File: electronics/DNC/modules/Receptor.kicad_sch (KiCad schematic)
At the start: 19 parts

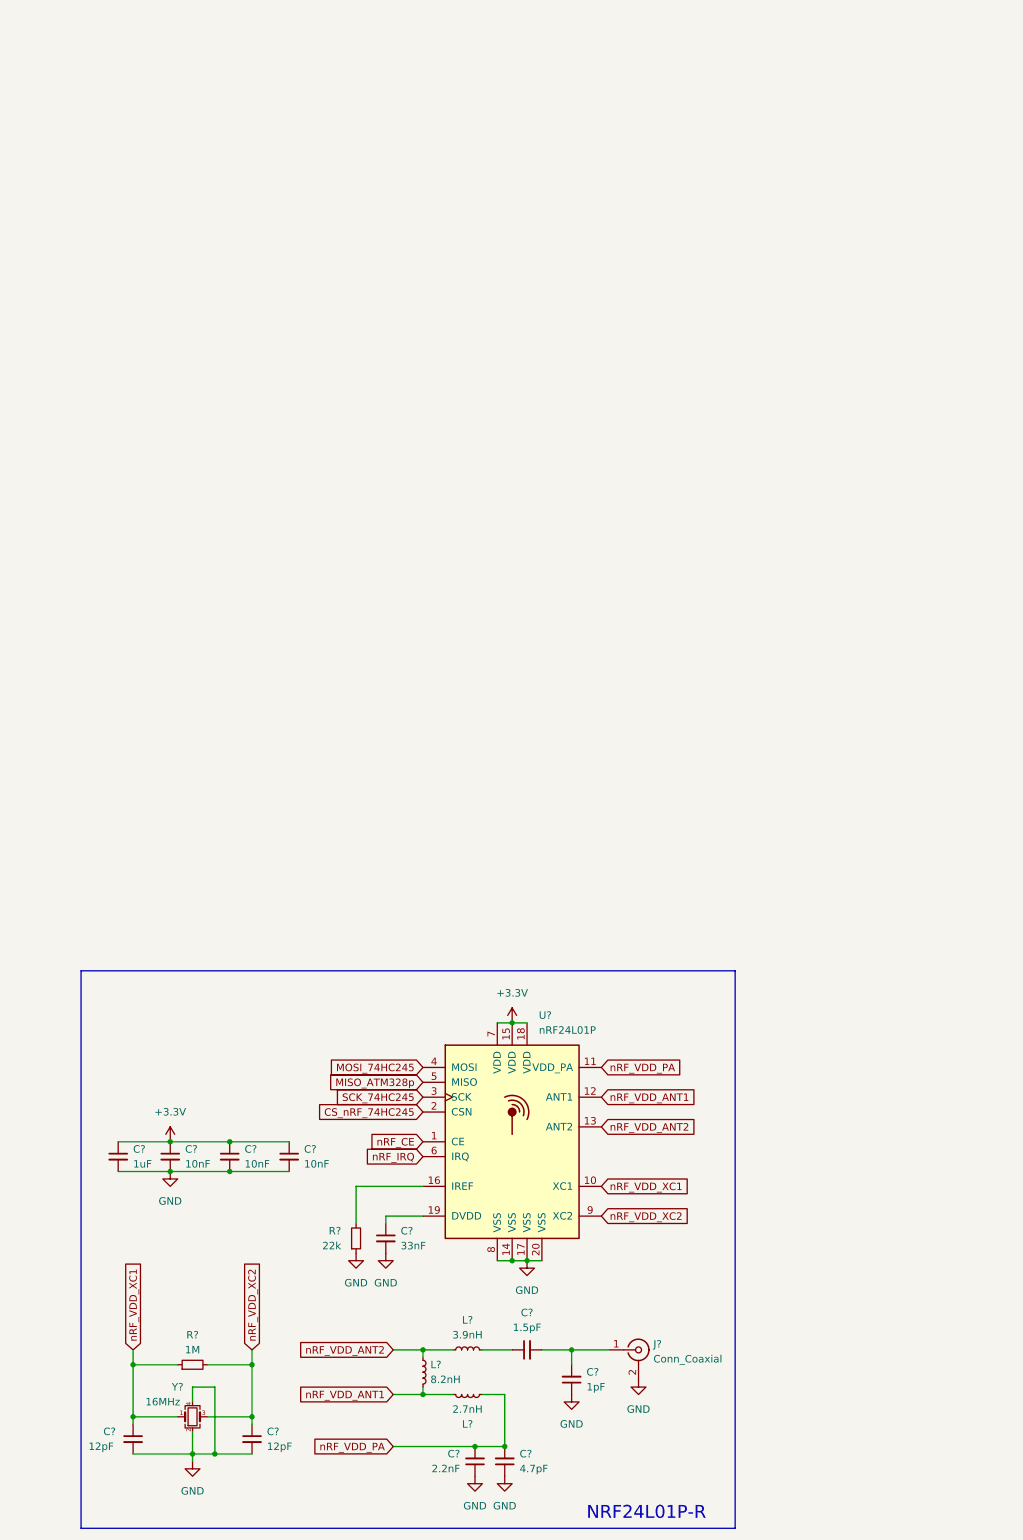
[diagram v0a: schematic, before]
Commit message: Se reemplazó la hoja del IMU por la de sensores y se agregó la hoja de indicadores
- Nueva hoja Sensores: IMU BMI270 (SPI1) y barómetro BMP581 (I2C1 propio, jumper BARO_ADDR).
- Nueva hoja Indicadores: buzzer piezo CPT-12123 con FDV303N y LEDs de estado en PB4/PB5.
- Se eliminó la hoja IMU.
- MicroSD por SDIO de 4 bits con filtro TPD6F002 y TVS ESD5Z3.3 en VDD.
- PMS: AP2112K en 3V3_SYS y LP5907 + ferrita en 3V3_SEN.
- Motores movidos a PA0-PA3 (TIM5) para liberar el SDIO.
- Arquitectura.drawio actualizado a la arquitectura v1 (ELRS por UART, sin OLED).
- Se agregó docs/RESUMEN_PROYECTO_DNC.md con decisiones y pendientes.

Co-Authored-By: Claude Opus 5.5 <noreply@anthropic.com>
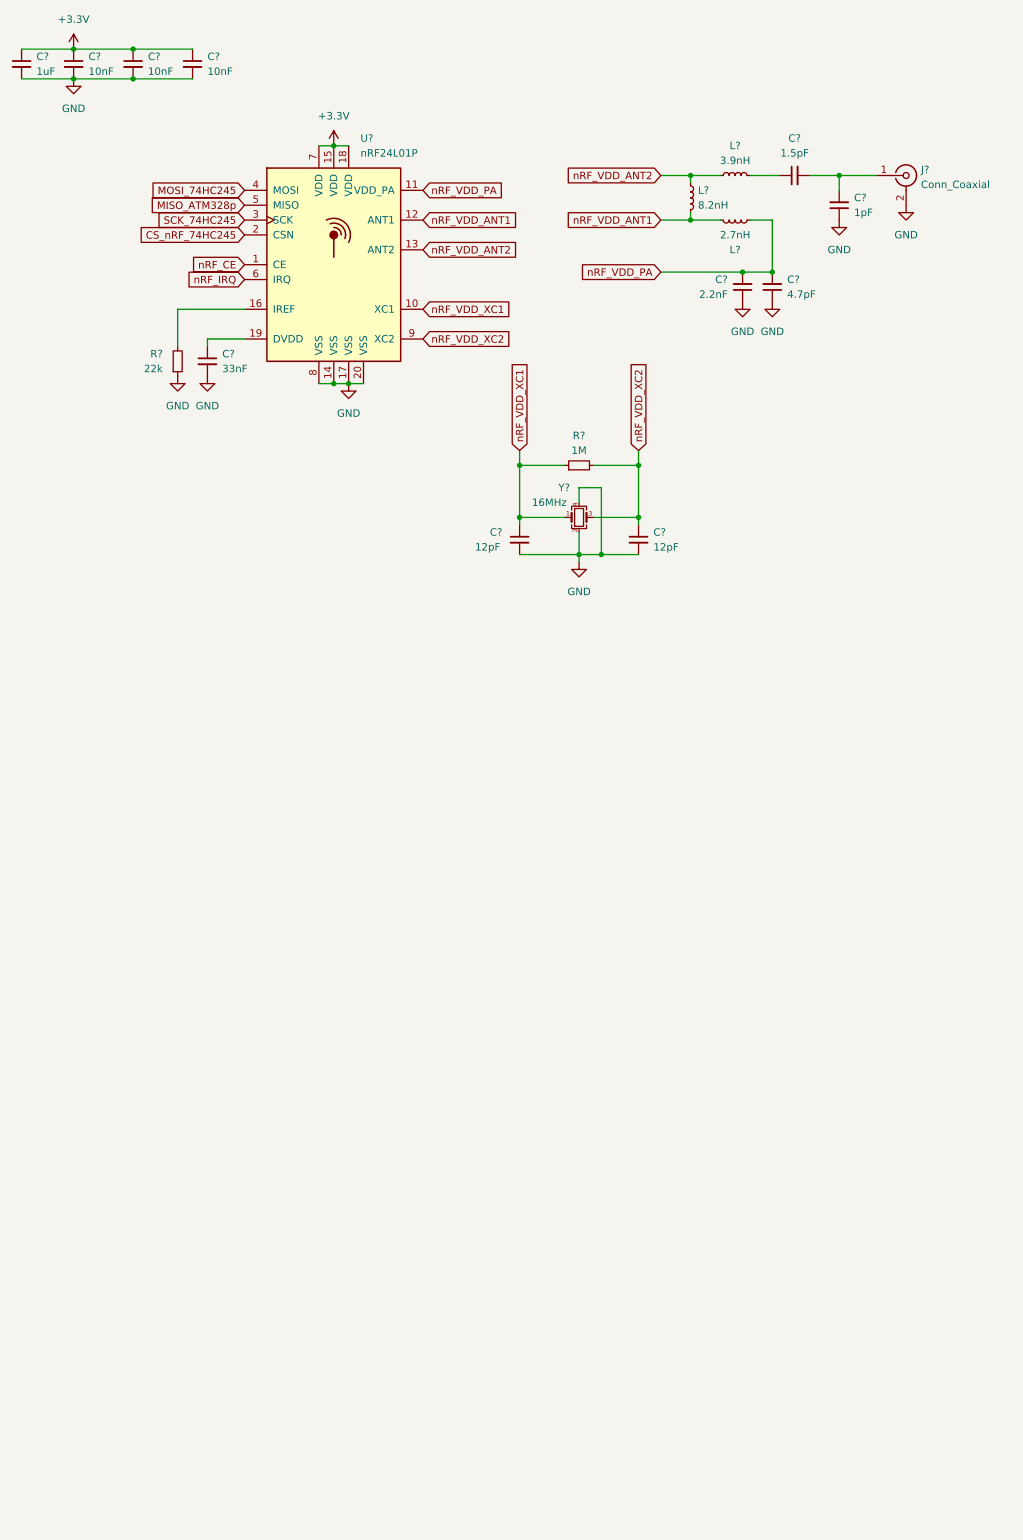
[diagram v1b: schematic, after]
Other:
- note removed: "NRF24L01P-R"
- moved on the sheet: C?, J?, L?, R?, U?, Y?
